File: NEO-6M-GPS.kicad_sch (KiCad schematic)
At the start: 3 parts, among them J7 20279-001E-03, U1 NEO-M8N, U6 NEO-6M-GPS

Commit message: Revision
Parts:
- removed U6: NEO-6M-GPS, footprints:XCVR_NEO-6M-GPS, symbol NEO-6M-GPS:NEO-6M-GPS
- renumbered J7 to J7CHECK
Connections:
- net +3V3: now also U1.2 (D_SEL), U1.23 (VCC)
- net GND: no longer U1.7 (VDD_USB)
- net TIMEPULSE: now also U1.3 (TIMEPULSE)
- net LNA_EN: now reaches U1.14 (LNA_EN)
- net GPS_RESET: now reaches U1.8 (~{RESET})
- net GPS_RXD1 renamed GPS_RX
- net GPS_TXD1 renamed GPS_TX
- no-connect marks 4 -> 9
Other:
- moved on the sheet: J7CHECK

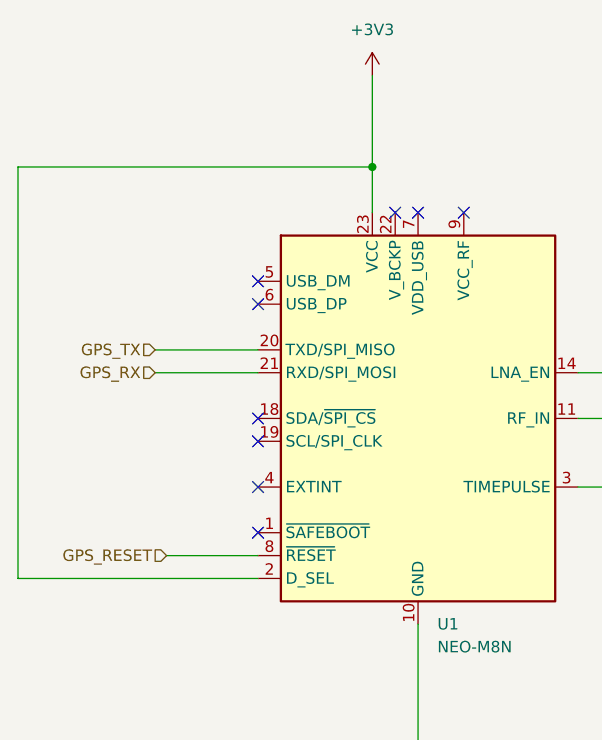
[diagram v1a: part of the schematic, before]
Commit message: update Schematic
Fixed N channel mosfet pyros and set to low side trigger
removed unneeded 5v buck converter
rerouted/optmized gpio pins
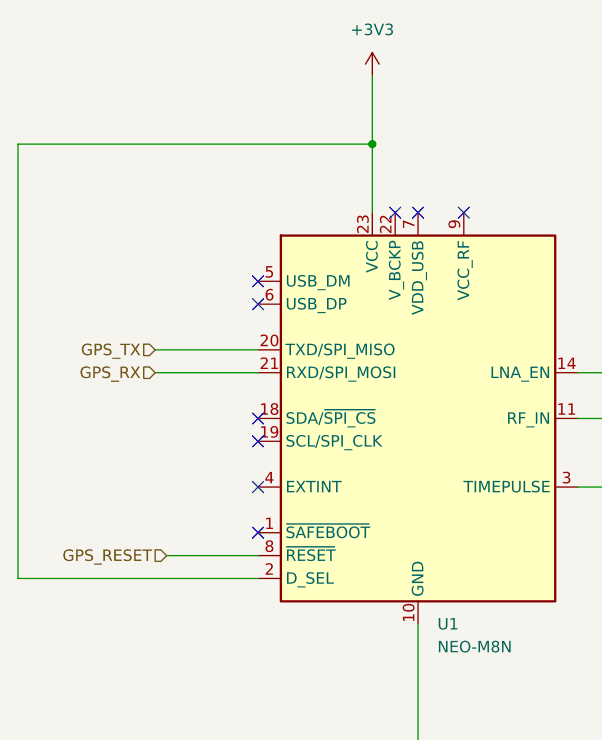
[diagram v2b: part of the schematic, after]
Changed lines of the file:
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@@
 	(generator "eeschema")
 	(generator_version "9.0")
-	(paper "A4")
+	(paper "A3")
 	(junction
-		(at 208.28 55.88)
+		(at 208.28 53.34)
 		(diameter 0)
 		(color 0 0 0 0)
@@
 	(wire
 		(pts
-			(xy 168.91 101.6) (xy 168.91 55.88)
+			(xy 168.91 101.6) (xy 168.91 53.34)
 		)
 		(stroke
@@
 	(wire
 		(pts
-			(xy 208.28 45.72) (xy 208.28 55.88)
+			(xy 208.28 45.72) (xy 208.28 53.34)
 		)
 		(stroke
@@
 	(wire
 		(pts
-			(xy 168.91 55.88) (xy 208.28 55.88)
+			(xy 168.91 53.34) (xy 208.28 53.34)
 		)
 		(stroke
@@
 	(wire
 		(pts
-			(xy 208.28 55.88) (xy 208.28 60.96)
+			(xy 208.28 53.34) (xy 208.28 60.96)
 		)
 		(stroke
